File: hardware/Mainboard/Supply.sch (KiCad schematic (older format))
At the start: 18 parts, among them IC8 TL7702A, SW1 RESET, SW8 FT232 RESET, U1 R-785.0-1.0, X1 DC IN, X5 GND

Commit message: Misc: 	- Update README 	- Add 74HC138 datasheet 	- Update board image 	- Add layout for website tutorial
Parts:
- added R14: 10k, Resistor_THT:R_Axial_DIN0207_L6.3mm_D2.5mm_P7.62mm_Horizontal, symbol Device:R
- added R15: 1k, Resistor_THT:R_Axial_DIN0207_L6.3mm_D2.5mm_P7.62mm_Horizontal, symbol Device:R
- X6: renamed from X5; Mfr. Amphenol FCI -> TE Connectivity / AMP; Mfr. No. 68001-400HLF -> 4-103327-3; Mouser 649-68001-400HLF -> 571-4-103327-3
- renumbered C9 to C13, C20 to C14, C10 to C15, C11 to C16, C12 to C17, C13 to C18, D10 to D11, D13 to D12, IC8 to IC11, R8 to R10, R5 to R11, R2 to R12, R11 to R9, SW8 to SW6, SW1 to SW7, X1 to X7
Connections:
- net ~Reset_FT232: now also R14.1; no longer SW6.2
- net at C16.1, IC11.2 (~RESIN), IC11.7 (SENSE)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: now also R15.1; no longer SW7.2
- new net: R14.2, SW6.2
- new net: R15.2, SW7.2
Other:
- moved on the sheet: C14, R11, R9

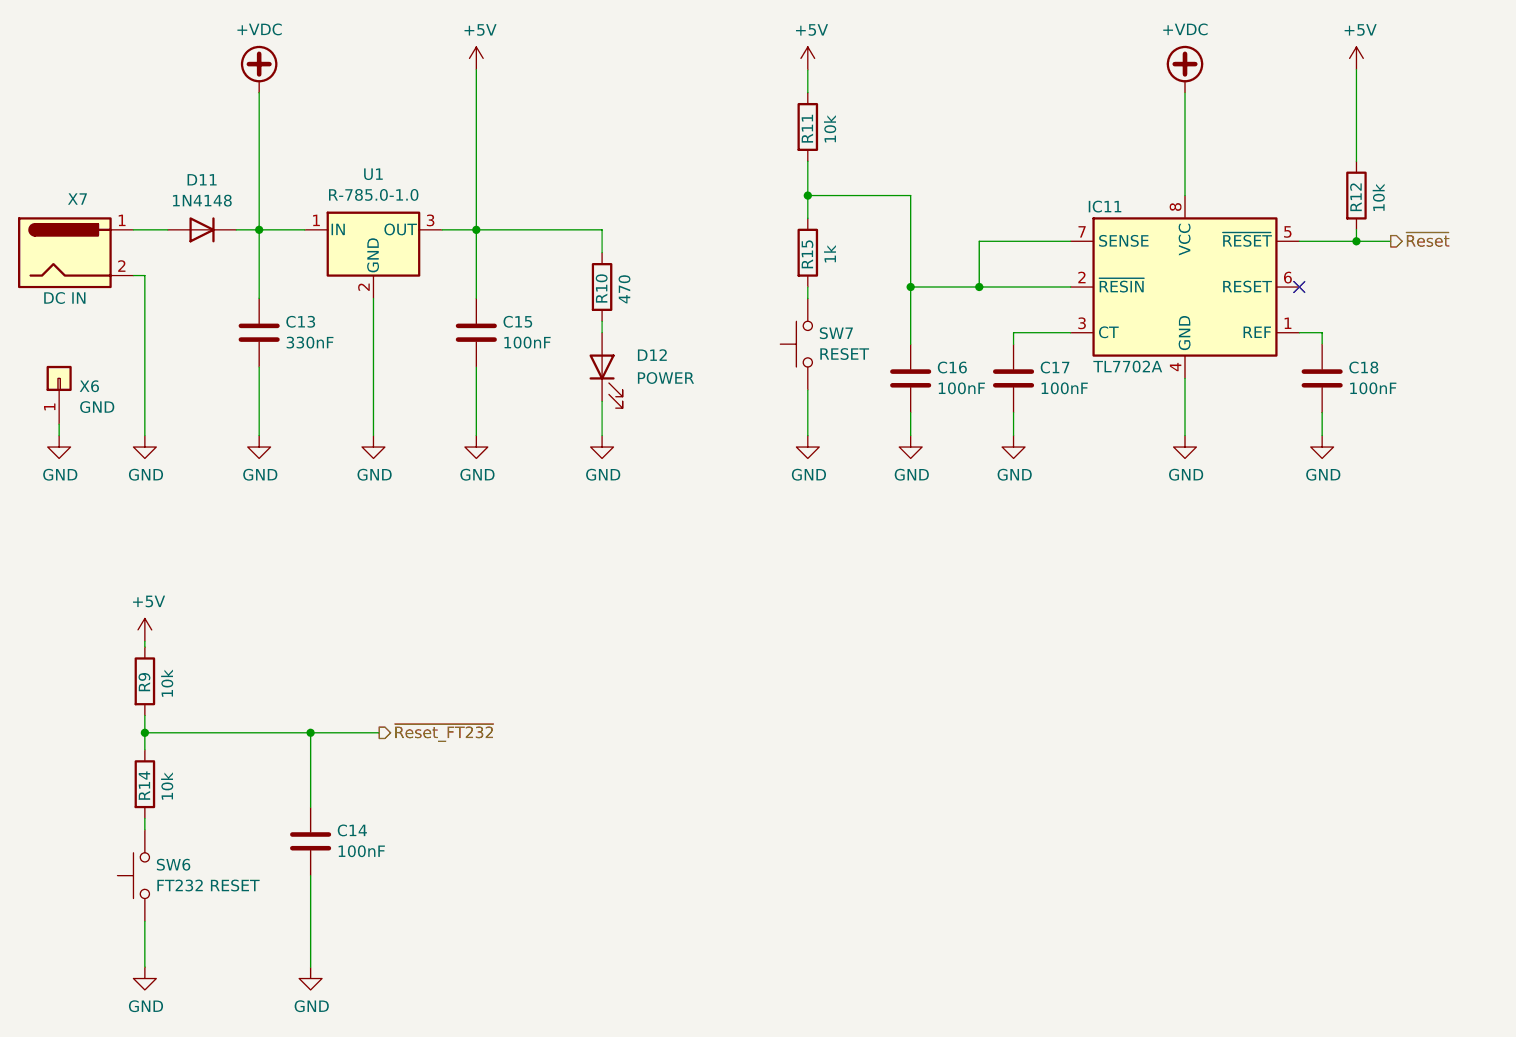
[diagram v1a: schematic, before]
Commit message: Hardware: 	- Add pull up resistor for PB
Documentation:
	- Add more datasheets
	- Update documentation

Misc:
	- Rename CHANGELOG
	- Remove old files

Signed-off-by: Daniel Kampert <DanielKampert@kampis-elektroecke.de>
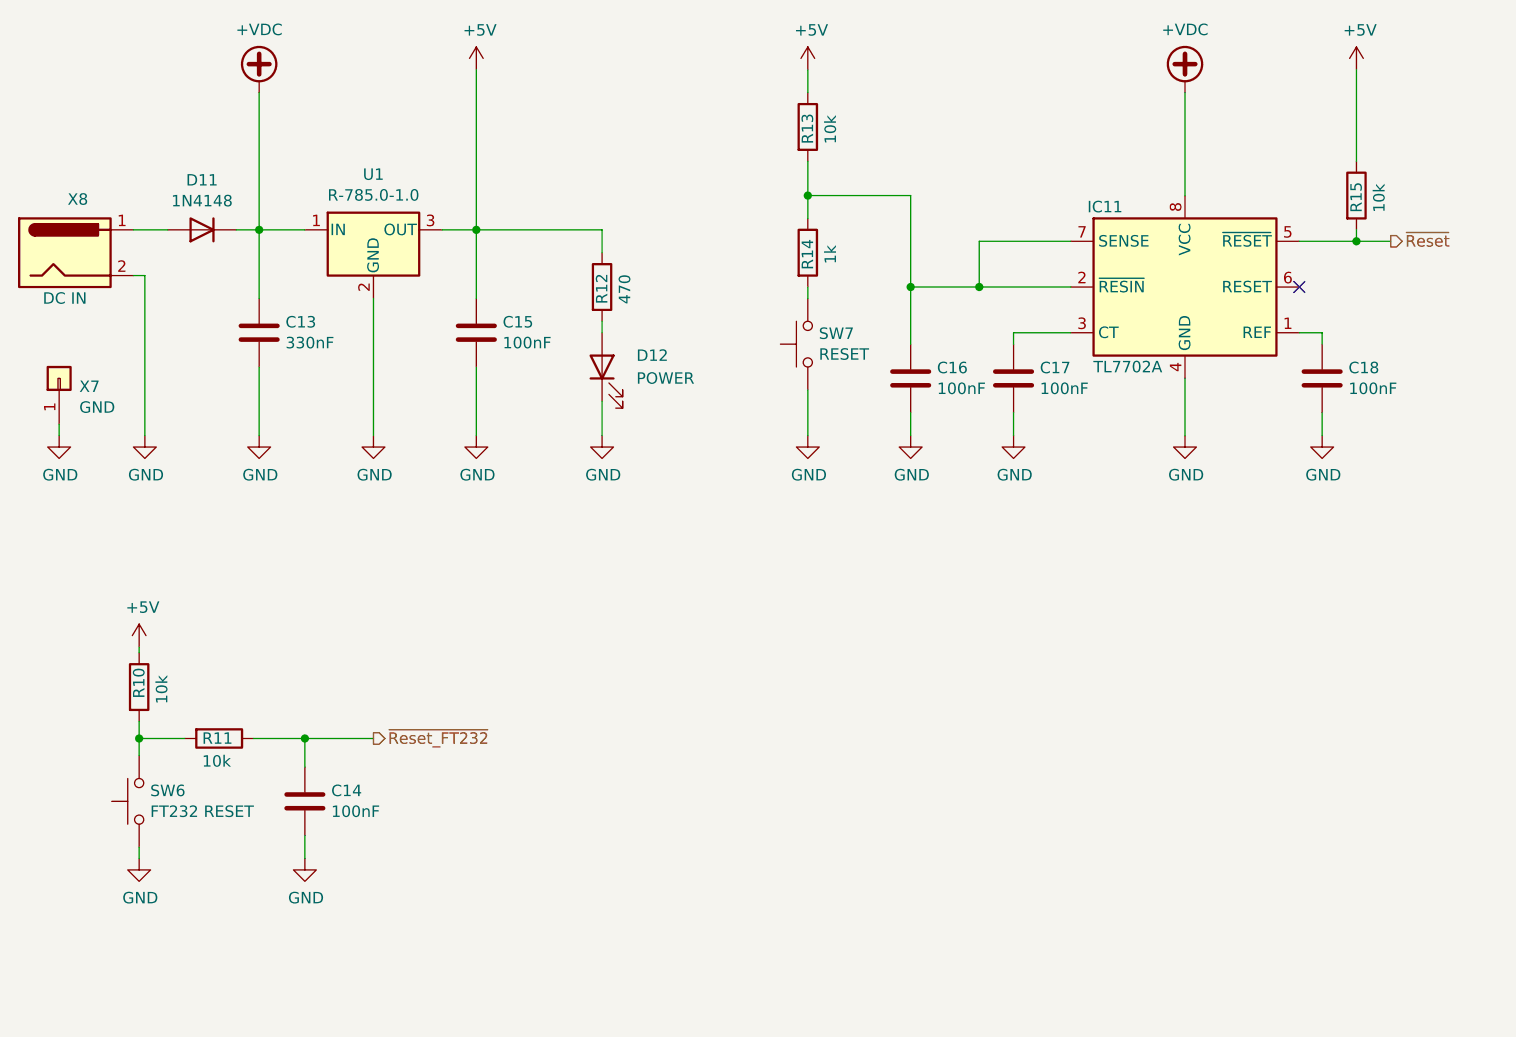
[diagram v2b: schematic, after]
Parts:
- C13: Distributor (none) -> Mouser; Order Number (none) -> 581-SR205E334MARTR1
- C14, C15, C16, C17, C18: Distributor (none) -> Mouser; Order Number (none) -> 810-FA18X8R1H104KRU6
- D11: Distributor (none) -> Mouser; Order Number (none) -> 512-1N4148
- D12: Distributor (none) -> Mouser; Order Number (none) -> 941-C503BRANCZ0C0AA1
- IC11: Distributor (none) -> Mouser; Order Number (none) -> 595-TL7702ACP
- R10: renamed from R9; Distributor (none) -> Mouser; Order Number (none) -> 603-MFP-25BRD52-10K
- R11: renamed from R14; Distributor (none) -> Mouser; Order Number (none) -> 603-MFP-25BRD52-10K
- R12: renamed from R10; Distributor (none) -> Mouser; Order Number (none) -> 603-MFP-25BRD52-470R
- R13: renamed from R11; Distributor (none) -> Mouser; Order Number (none) -> 603-MFP-25BRD52-10K
- R14: renamed from R15; Distributor (none) -> Mouser; Order Number (none) -> 603-MFP-25BRD52-1K
- R15: renamed from R12; Distributor (none) -> Mouser; Order Number (none) -> 603-MFP-25BRD52-10K
- SW6, SW7: Distributor (none) -> Mouser; Order Number (none) -> 506-2-1825910-7
- U1: Distributor (none) -> Mouser; Order Number (none) -> 919-R-785.0-1.0
- X7: renamed from X6; Distributor (none) -> Mouser; Order Number (none) -> 571-4-103327-3
- X8: renamed from X7; Distributor (none) -> Mouser; Order Number (none) -> 710-694106301002
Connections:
- net ~Reset_FT232: no longer R10.2
- net at R11.2, SW6.2: now also R10.2
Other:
- moved on the sheet: C14, R10, R11, SW6
